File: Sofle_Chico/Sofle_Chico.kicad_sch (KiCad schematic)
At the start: 108 parts, among them J1 Conn_01x04, J2 Conn_01x04, J3 Conn_01x04, J4 MJ-4PP-9, J5 Conn_01x05, J6 Conn_01x05, J7 Conn_01x05, SW1 SW_PUSH, SW10 SW_PUSH, SW11 SW_PUSH, SW12 SW_PUSH, SW13 SW_PUSH, SW14 SW_PUSH, SW15 SW_PUSH, SW16 SW_PUSH, SW17 SW_PUSH, SW18 SW_PUSH, SW19 Rotary_Encoder_Switch-Device, SW2 SW_PUSH, SW20 SW_PUSH, SW21 SW_PUSH, SW22 SW_PUSH, SW23 SW_PUSH, SW24 SW_PUSH, SW25 SW_PUSH, SW26 SW_PUSH, SW27 SW_PUSH, SW28 SW_PUSH, SW29 SW_PUSH, SW3 SW_PUSH, SW30 SW_PUSH, SW4 SW_PUSH, SW5 SW_PUSH, SW6 SW_PUSH, SW7 SW_PUSH, SW8 SW_PUSH, SW9 SW_PUSH, U1 SN74AHCT1G125, U2 Pico

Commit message: Painfully figuring out how to Fork and unfork myself
Fixed busted footprints and lost SCH changes from Git goof-ups. Discovering what I've failed to properly put into version control & tinkering
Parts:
- added JP2: SolderJumper_2_Open, symbol Sofle_Pico:SolderJumper_2_Open
- added Q1: DMG2305UX, Package_TO_SOT_SMD_AKL:SOT-23, symbol PCM_Transistor_MOSFET_AKL:DMG2305UX
- LED1, LED10, LED11, LED12, LED13, LED14, LED15, LED16, LED17, LED18, LED19, LED2, LED20, LED21, LED22, LED23, LED24, LED25, LED26, LED27, LED28, LED29, LED3, LED4, LED5, LED6, LED7, LED8, LED9: footprint Sofle_Chico:SK6803_MINIE_v2 -> Sofle_Pico:SK6803_MINI-E_V2
- SW25: footprint Sofle_Pico:SW_Hotswap_Kailh_Choc_V1V2_DS_1.00u_1 -> Sofle_Pico:RotaryEncoder_Alps_EC11E-Switch_Vertical_H20mm-keebio_modified
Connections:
- net at LED25.2 (DIN): now also LED24.4 (DOUT); no longer LED19.4 (DOUT)
- net at LED12.4 (DOUT): now also LED13.2 (DIN); no longer LED6.2 (DIN)
- net at LED6.4 (DOUT): now also LED7.2 (DIN)
- net at LED1.4 (DOUT): now also LED2.2 (DIN); no longer LED7.2 (DIN)
- net at LED7.4 (DOUT): now also LED8.2 (DIN); no longer LED13.2 (DIN)
- net at LED22.2 (DIN): now also LED21.4 (DOUT); no longer LED29.4 (DOUT)
- net at LED9.2 (DIN): now also LED8.4 (DOUT); no longer LED3.4 (DOUT)
- net at LED15.2 (DIN): now also LED14.4 (DOUT); no longer LED9.4 (DOUT)
- net at LED11.2 (DIN): now also LED10.4 (DOUT); no longer LED5.4 (DOUT)
- net at LED17.2 (DIN): now also LED16.4 (DOUT); no longer LED11.4 (DOUT)
- net at LED28.2 (DIN): now also LED27.4 (DOUT); no longer LED21.4 (DOUT)
- net at LED20.2 (DIN): now also LED19.4 (DOUT); no longer LED27.4 (DOUT)
- net at LED14.2 (DIN): now also LED13.4 (DOUT); no longer LED20.4 (DOUT)
- net at LED18.2 (DIN): now also LED17.4 (DOUT); no longer LED24.4 (DOUT)
- net at LED23.2 (DIN): now also LED22.4 (DOUT); no longer LED17.4 (DOUT)
- net at LED12.2 (DIN): now also LED11.4 (DOUT); no longer LED18.4 (DOUT)
- net VBUS: now reaches D31.2 (A), U2.40 (VBUS)
- net VBUS: now also Q1.1 (G)
- net at LED16.2 (DIN): now also LED15.4 (DOUT); no longer LED22.4 (DOUT)
- net at LED10.2 (DIN): now also LED9.4 (DOUT); no longer LED16.4 (DOUT)
- net at LED4.2 (DIN): now also LED3.4 (DOUT); no longer LED10.4 (DOUT)
- net at LED19.2 (DIN): now also LED18.4 (DOUT); no longer LED13.4 (DOUT)
- net at LED21.2 (DIN): now also LED20.4 (DOUT); no longer LED15.4 (DOUT)
- net +5V renamed VCC
- net VCC: now also JP2.2 (B), Q1.2 (S); no longer J4.2, U1.5 (VCC)
- new net: J4.2, JP2.1 (A), Q1.3 (D)
- new net: LED5.4 (DOUT), LED6.2 (DIN)

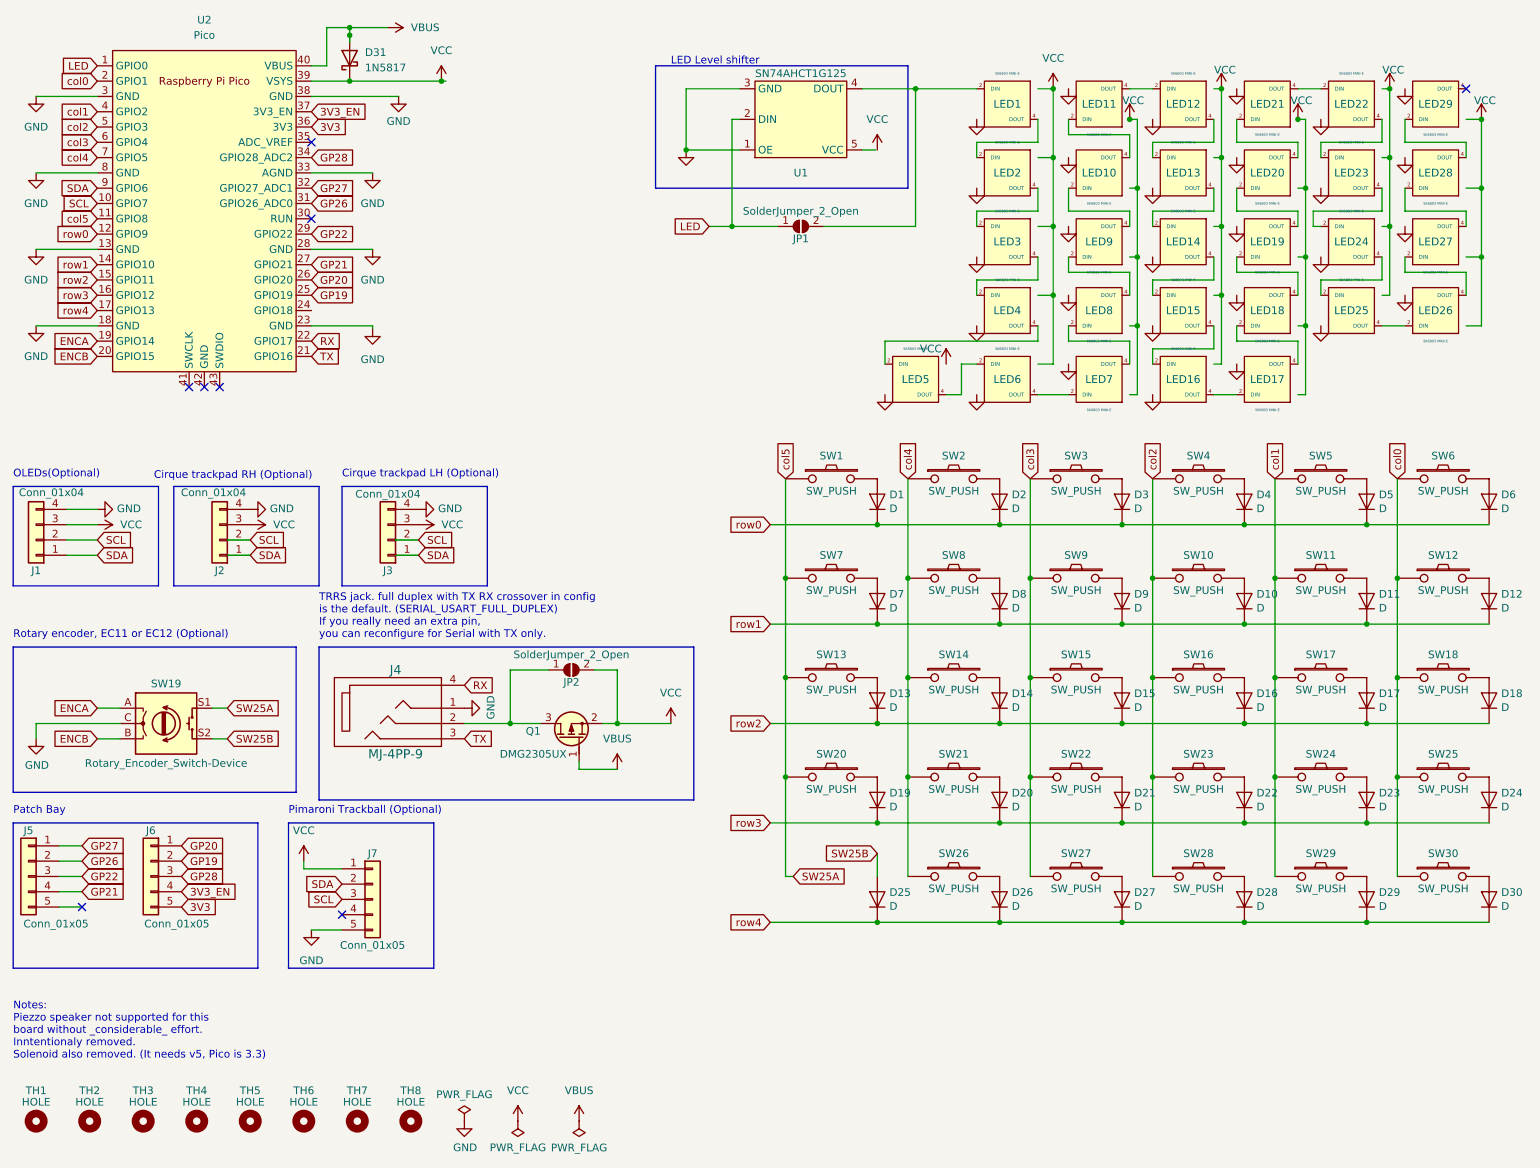
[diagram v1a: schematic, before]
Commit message: Routing progress.
Cleaned up STEP model links for relative paths

Implemented first pass at PFET power-split protection

tinkering with LED footprints

Fixed unintentionally altered annotation
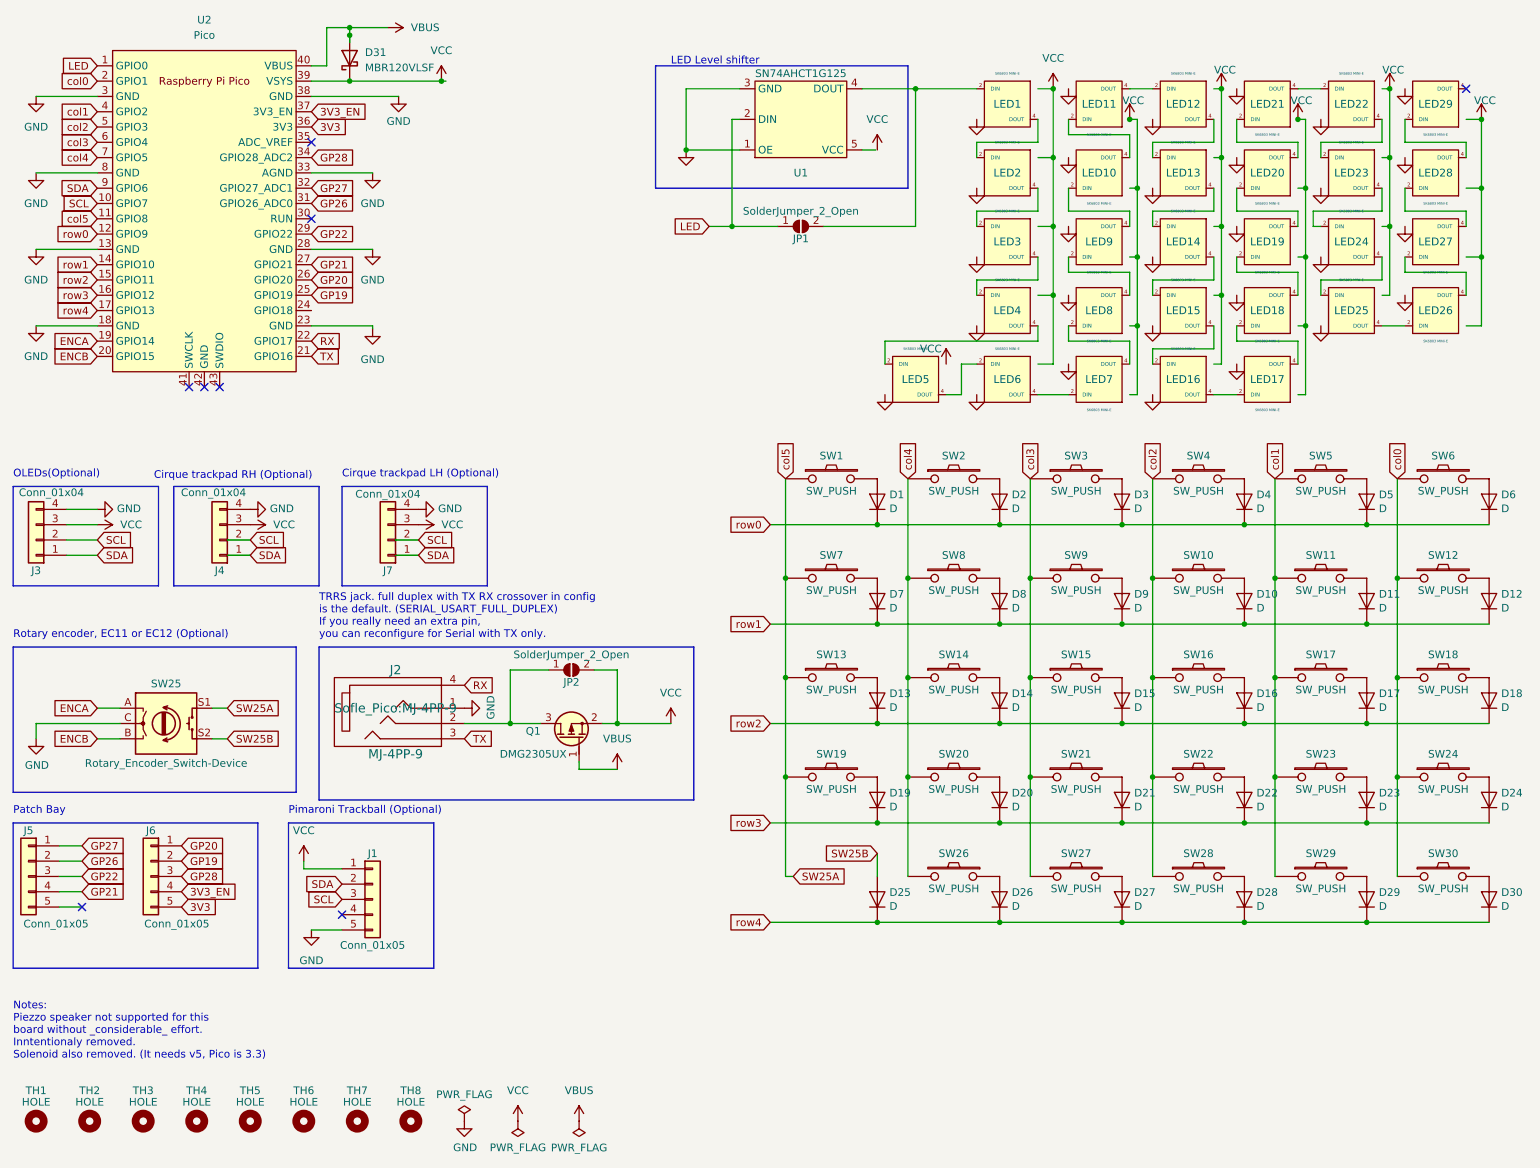
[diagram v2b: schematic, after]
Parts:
- removed SW25: SW_PUSH, Sofle_Pico:RotaryEncoder_Alps_EC11E-Switch_Vertical_H20mm-keebio_modified, symbol Sofle_Pico:SW_PUSH
- added SW20: SW_PUSH, Sofle_Pico:SW_Hotswap_Kailh_Choc_V1V2_DS_1.00u_1, symbol Sofle_Pico:SW_PUSH
- D31: value 1N5817 -> MBR120VLSF; footprint Diode_THT:D_DO-41_SOD81_P10.16mm_Horizontal -> Sofle_Pico:D_SOD-123_DO-41_Hybrid_DoubleSided_V2_1
- J1: renamed from J7; footprint (none) -> Sofle_Pico:Pimaroni_PinHeader_1x05_P2.54mm_Vertical Sofle v3b
- J2: renamed from J4; footprint (none) -> Sofle_Pico:MJ-4PP-9
- J3: renamed from J1; footprint (none) -> Sofle_Pico:OLED SSD1306 128x64
- J4: renamed from J2; footprint (none) -> Sofle_Pico:Cirque tie in
- J5: footprint (none) -> Sofle_Pico:PinHeader_1x05_P2.54mm_Vertical_one-dead
- J6: footprint (none) -> Sofle_Pico:PinHeader_1x05_P2.54mm_Vertical
- J7: renamed from J3; footprint (none) -> Sofle_Pico:Cirque tie in
- JP1, JP2: footprint (none) -> Sofle_Pico:Level Shifter Bypass Jumper
- Q1: footprint Package_TO_SOT_SMD_AKL:SOT-23 -> Package_TO_SOT_SMD:SOT-23-3
- SW25: renamed from SW19; footprint (none) -> Sofle_Pico:RotaryEncoder_Alps_EC11E-Switch_Vertical_H20mm-keebio_modified
- U1: footprint Junco:SN74AHCT1G125 -> PCM_Package_TO_SOT_SMD_AKL:SOT-23-5_HandSoldering
- renumbered SW20 to SW19
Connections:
- net col0: now also SW24.1
- net col1: now also SW23.1; no longer SW24.1
- net col2: now also SW22.1; no longer SW23.1
- net col3: now also SW21.1; no longer SW22.1
- net col4: now also SW26.2, SW20.1; no longer SW21.1, SW26.1
- net at D26.2 (A): now also SW26.1; no longer SW26.2
- net at D21.2 (A): now also SW21.2; no longer SW22.2
- net at D22.2 (A): now also SW22.2; no longer SW23.2
- net at D23.2 (A): now also SW23.2; no longer SW24.2
- net at D24.2 (A): now also SW24.2
- net at D20.2 (A): now also SW20.2; no longer SW21.2

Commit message: VBUS / VSYS Diode sod123 option for D31 implemented J4 power PFET protection implemented Swapped Bot fill to GND and Top Fill to VCC, improved power islands and removed floating copper Began row/column wiring to figure out power flow / signal return considerations
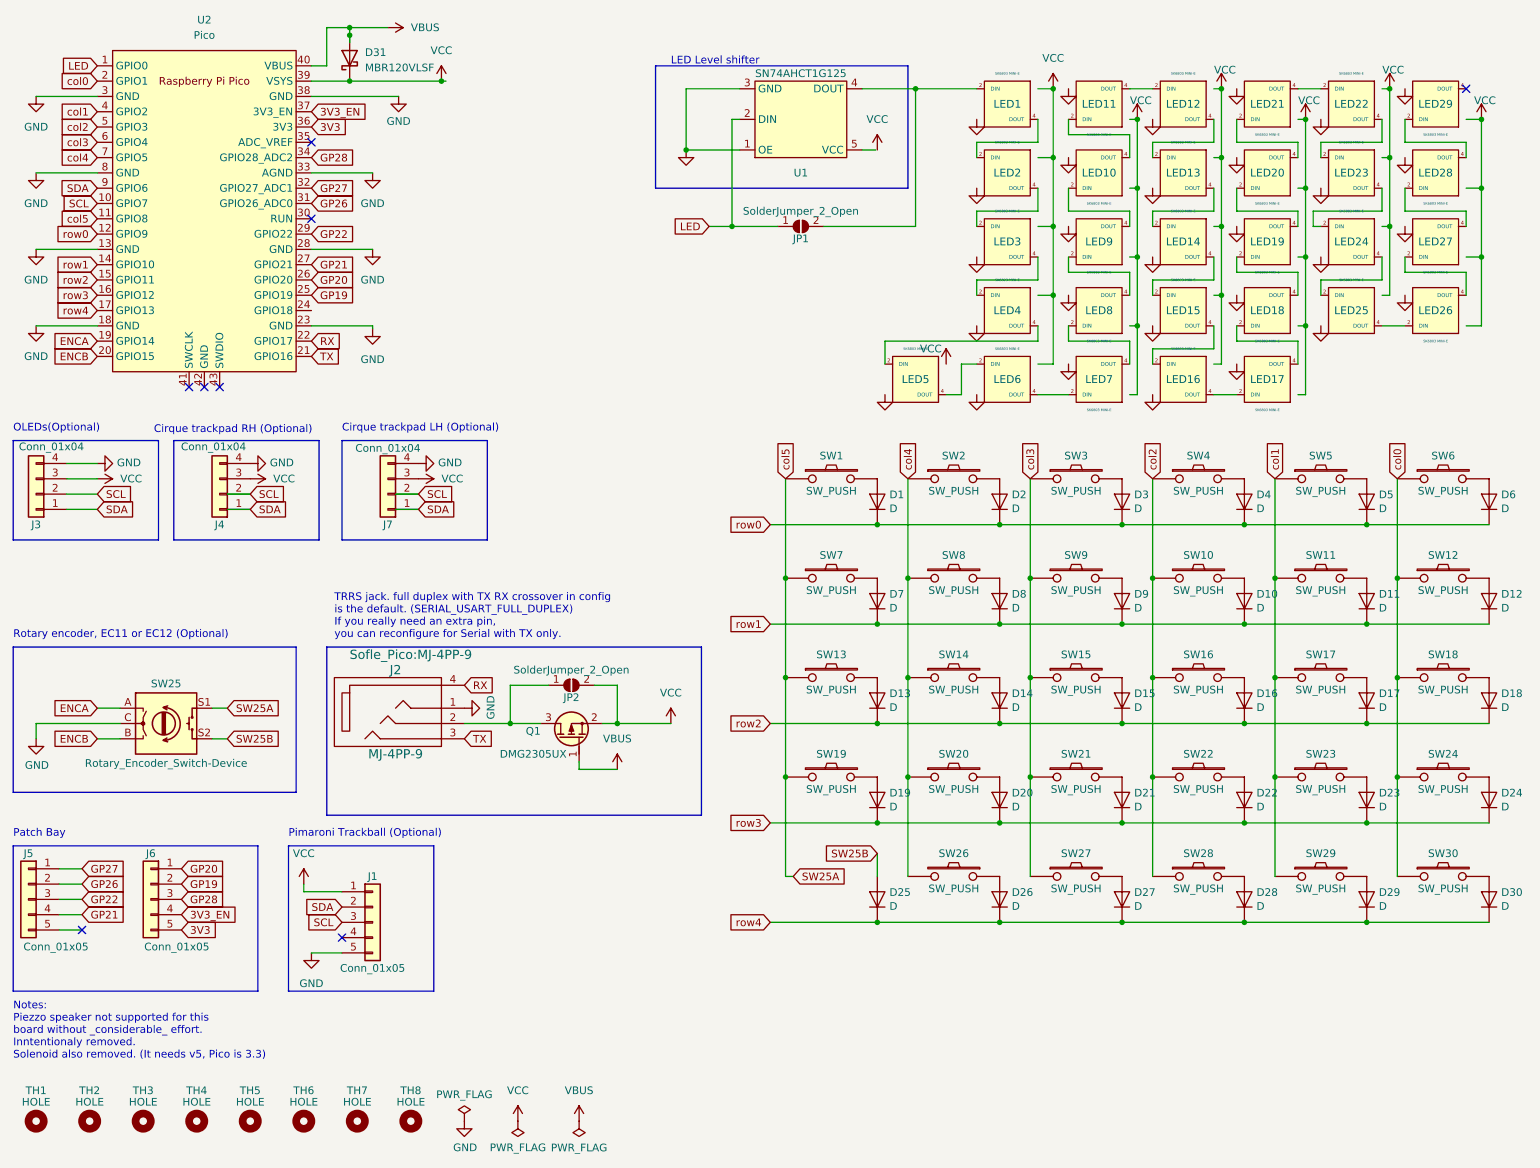
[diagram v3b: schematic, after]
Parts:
- D31: footprint Sofle_Pico:D_SOD-123_DO-41_Hybrid_DoubleSided_V2_1 -> Sofle_Pico:D_SOD-123_DO-41_7.62mm_Hybrid_DoubleSided
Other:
- moved on the sheet: J1, J3, J4, J5, J6, J7, JP2

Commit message: Routing progress, dual-sided the SOT-23 PFET footprint
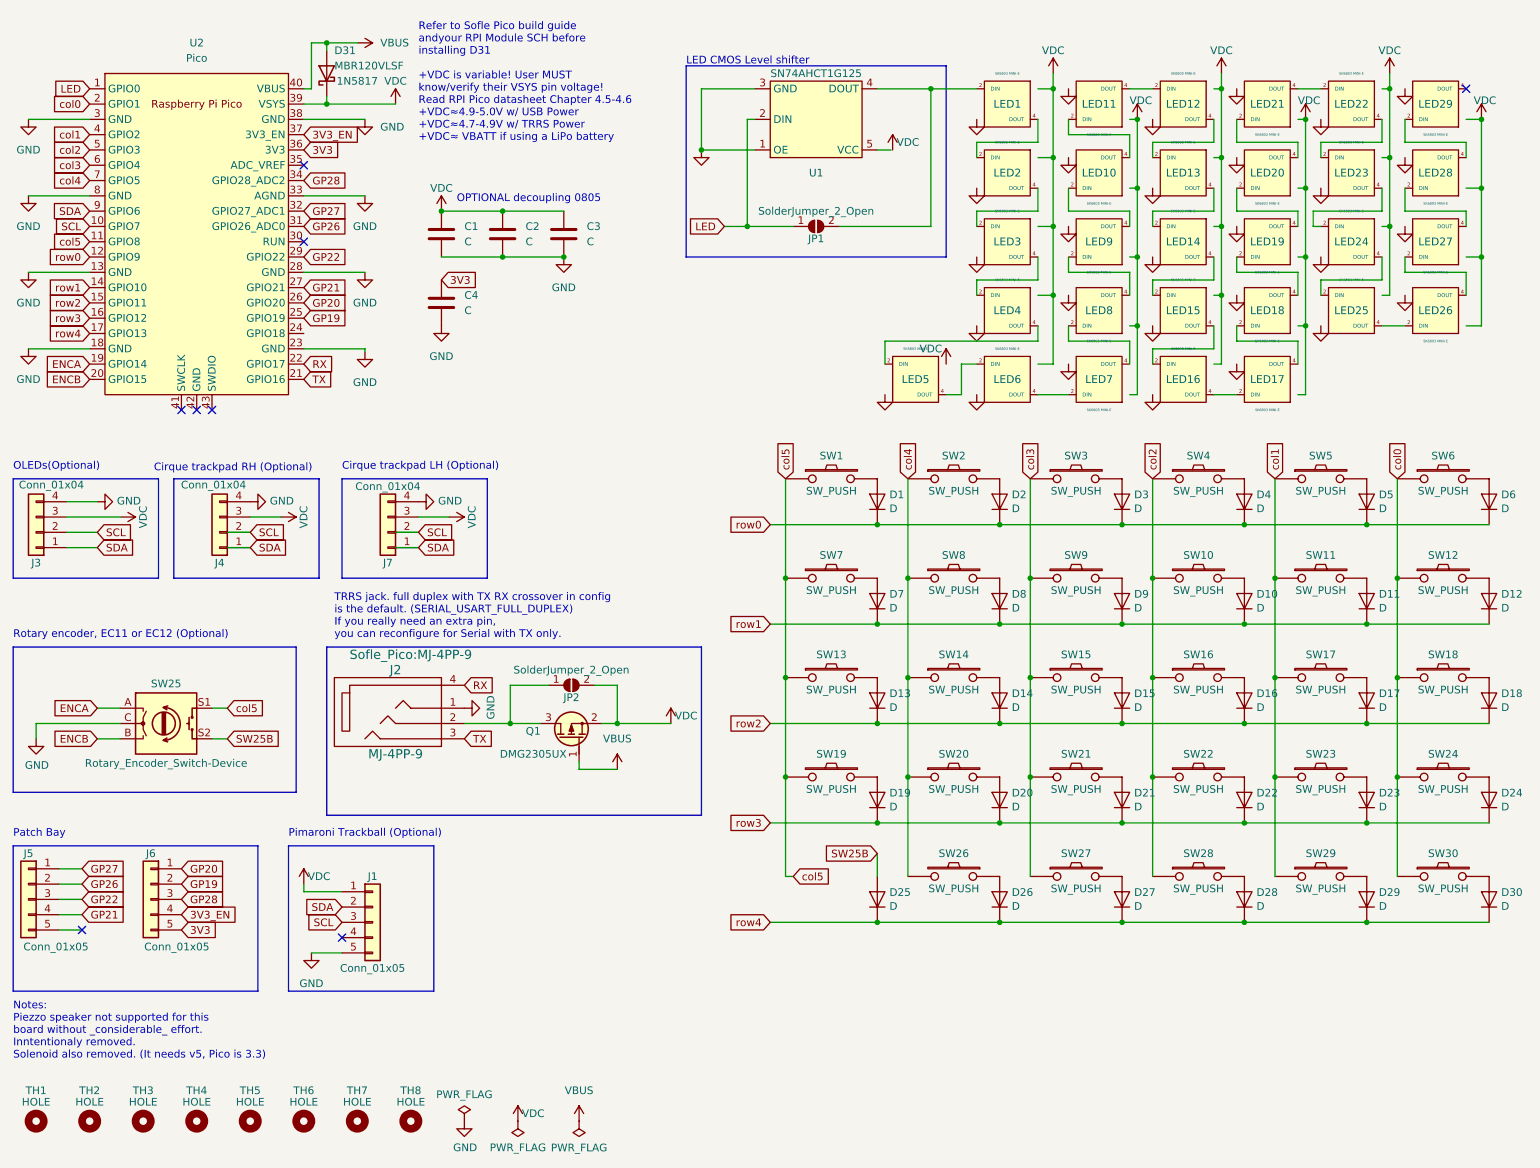
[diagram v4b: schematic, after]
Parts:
- added C1, C2, C3, C4: C, Capacitor_SMD:C_0805_2012Metric_Pad1.18x1.45mm_HandSolder, symbol Device:C
- D31: TH_Val (none) -> 1N5817
- Q1: footprint Package_TO_SOT_SMD:SOT-23-3 -> Sofle_Pico:SOT-23_DS
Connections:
- net 3V3: now also C4.1
- net GND: now also C1.2, C2.2, C3.2, C4.2
- net SW25A renamed col5
- net VCC renamed VDC
- net VDC: now also C1.1, C2.1, C3.1
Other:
- note added: "LED CMOS Level shifter"
- note added: "OPTIONAL decoupling 0805"
- note added: "Refer to Sofle Pico build guide andyour RPI Module SCH before installing D31 +VDC is variable! User MUST know/verify their VSYS pin voltage! Read RPI Pico datasheet Chapter 4.5-4.6 +VDC≈4.9-5.0V w/ USB Power +VDC≈4.7-4.9V w/ TRRS Power +VDC≈ VBATT if using a LiPo battery"
- note removed: "LED Level shifter"
- moved on the sheet: D31, J3, J4, J7, JP1, U1, U2
